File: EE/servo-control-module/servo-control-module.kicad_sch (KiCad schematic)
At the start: 4 parts, among them J1 SERVO, J2 USB, U1 ATtiny85-20P

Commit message: Updates for first milled board.
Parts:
- J1: footprint Connector_PinHeader_1.27mm:PinHeader_1x03_P1.27mm_Vertical -> Connector_PinHeader_2.54mm:PinHeader_1x03_P2.54mm_Vertical
- J2: footprint Connector_PinHeader_1.27mm:PinHeader_1x05_P1.27mm_Vertical -> Connector_PinSocket_2.54mm:PinSocket_1x05_P2.54mm_Vertical
- RV1: footprint Potentiometer_THT:Potentiometer_Vishay_148-149_Single_Horizontal -> Potentiometer_THT:Potentiometer_Alps_RK163_Single_Horizontal
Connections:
- net SERVO: now also U1.7 (PB2); no longer U1.6 (PB1)

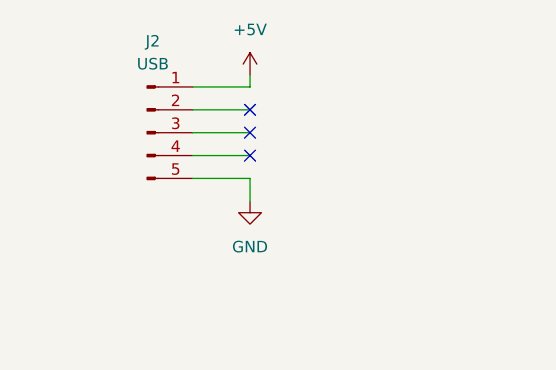
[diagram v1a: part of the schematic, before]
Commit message: Added footprint and 3D model for USB breakout adapter.
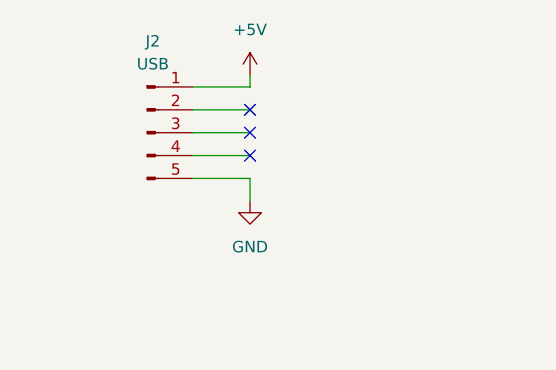
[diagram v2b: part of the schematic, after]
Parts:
- J2: footprint Connector_PinSocket_2.54mm:PinSocket_1x05_P2.54mm_Vertical -> Library:USB-micro-breakout
- RV1: footprint Potentiometer_THT:Potentiometer_Alps_RK163_Single_Horizontal -> Library:Potentiometer_Amazon_Single_Horizontal
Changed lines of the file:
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@@
       (effects (font (size 1.27 1.27)))
     )
-    (property "Footprint" "Connector_PinSocket_2.54mm:PinSocket_1x05_P2.54mm_Vertical" (at 46.99 45.72 0)
+    (property "Footprint" "Library:USB-micro-breakout" (at 46.99 45.72 0)
       (effects (font (size 1.27 1.27)) hide)
     )
@@
       (effects (font (size 1.27 1.27)) (justify right))
     )
-    (property "Footprint" "Potentiometer_THT:Potentiometer_Alps_RK163_Single_Horizontal" (at 125.73 92.71 0)
+    (property "Footprint" "Library:Potentiometer_Amazon_Single_Horizontal" (at 125.73 92.71 0)
       (effects (font (size 1.27 1.27)) hide)
     )

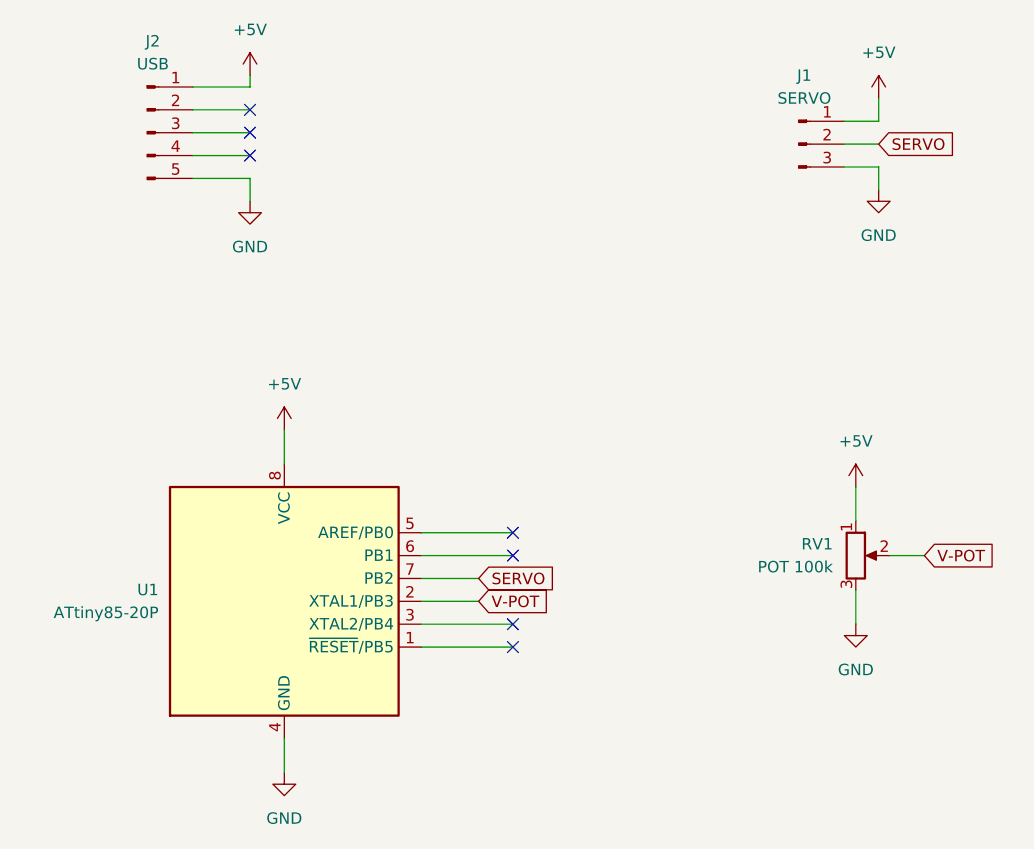
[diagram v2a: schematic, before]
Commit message: Updated to KiCad v8
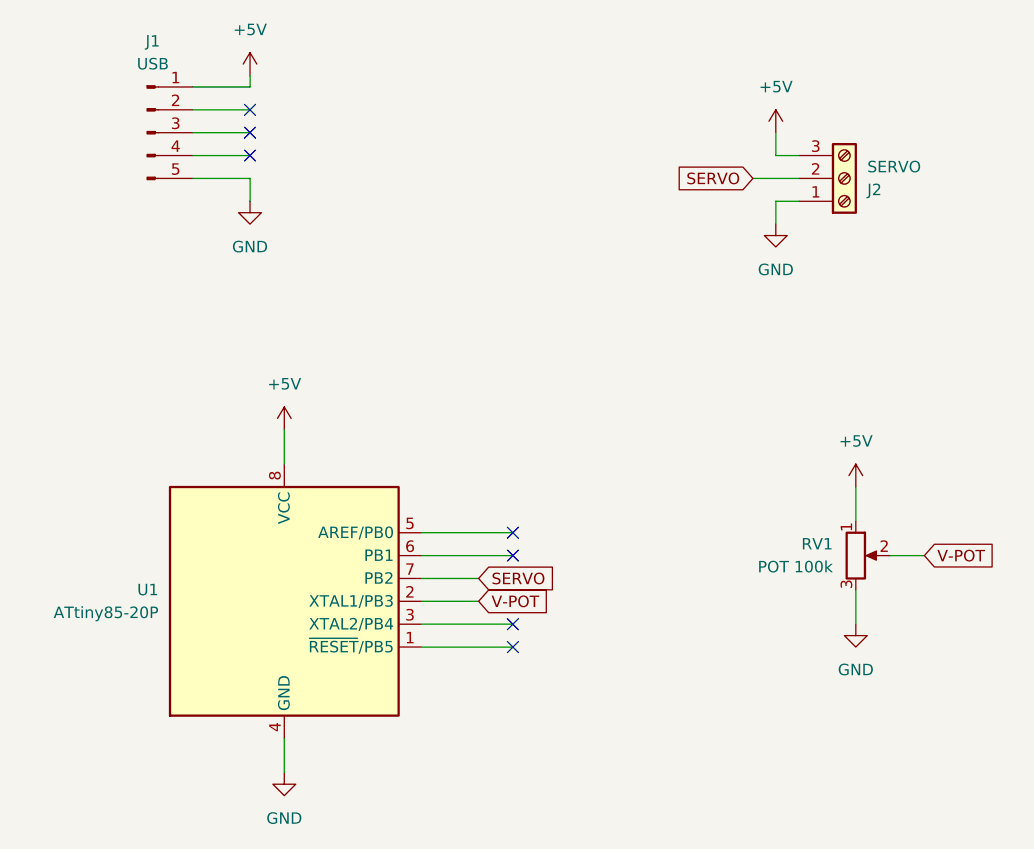
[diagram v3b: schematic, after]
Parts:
- removed J1: SERVO, Connector_PinHeader_2.54mm:PinHeader_1x03_P2.54mm_Vertical, symbol Connector:Conn_01x03_Pin
- added J2: SERVO, TerminalBlock_TE-Connectivity:TerminalBlock_TE_282834-3_1x03_P2.54mm_Horizontal, symbol Connector:Screw_Terminal_01x03
- renumbered J2 to J1
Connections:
- net +5V: now also J2.3 (Pin_3)
- net GND: now also J2.1 (Pin_1)
- net SERVO: now also J2.2 (Pin_2)
